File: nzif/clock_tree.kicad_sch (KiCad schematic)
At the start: 63 parts, among them J111 SMA, U128 ABLNO-VCXO, U129 AD9523-1BCPZ, U130 SN74AUC16374DGGR, U131 SN74LVC8T245, U132 SN74CBTLV3253, U133 SN74CBTLV3253, U134 SN74LVC8T245, X101 CTS_535_TCXO

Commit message: wire top sheet from rf front end through rx driver amps
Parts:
- renumbered C233 to C701, C234 to C702, C235 to C703, C236 to C704, C237 to C705, C238 to C706, C239 to C707, C240 to C708, C241 to C709, C242 to C710, C243 to C711, C244 to C712, C245 to C713, C246 to C714, C247 to C715, C248 to C716, C249 to C717, C251 to C718, C252 to C719, C254 to C720, C255 to C721, C250 to C722, C253 to C723, C257 to C724, C258 to C725, C256 to C726, C259 to C727, C260 to C728, C261 to C729, C262 to C730, C264 to C731, C263 to C732, C266 to C733, C265 to C734, C267 to C735, C268 to C736, C269 to C737, C270 to C738, C271 to C739, C272 to C740, C273 to C741, C274 to C742, C275 to C743, C276 to C744, C277 to C745, C278 to C746, C279 to C747, C280 to C748, C281 to C749, J111 to J701, R181 to R701, R182 to R702, R183 to R703, R184 to R704, TR103 to TR701, U128 to U701, U129 to U702, U130 to U703, U131 to U704, U132 to U705, U133 to U706, U134 to U707, X101 to X701

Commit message: updates to top level
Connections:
- net UC_CLK: no longer names the net of U702.53 (OUT4)
- no-connect marks 31 -> 32
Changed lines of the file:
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@@
 	)
 	(no_connect
+		(at 186.69 74.93)
+	)
+	(no_connect
 		(at 186.69 41.91)
 	)
@@
 		)
 	)
-	(hierarchical_label "UC_CLK"
-		(shape output)
-		(at 186.69 74.93 0)
-		(effects
-			(font
-				(size 1.27 1.27)
-			)
-			(justify left)
-		)
-	)

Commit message: minor schematic fixes
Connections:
- net LDO_VCO: now also C726.1
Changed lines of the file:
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@@
-	(wire
-		(pts
-			(xy 69.85 72.39) (xy 81.28 72.39)
-		)
-		(stroke
-			(width 0)
-			(type default)
-		)
-	)
 	(wire
 		(pts
@@
 		(pts
 			(xy 255.27 237.49) (xy 255.27 240.03)
+		)
+		(stroke
+			(width 0)
+			(type default)
+		)
+	)
+	(wire
+		(pts
+			(xy 78.74 72.39) (xy 90.17 72.39)
 		)
 		(stroke
@@
 	)
 	(label "1.8V"
-		(at 123.19 151.13 0)
+		(at 106.68 151.13 0)
 		(effects
 			(font
@@
 	)
 	(label "3.3V"
-		(at 123.19 186.69 0)
-		(effects
-			(font
+		(at 107.95 186.69 0)
+		(effects
+			(font

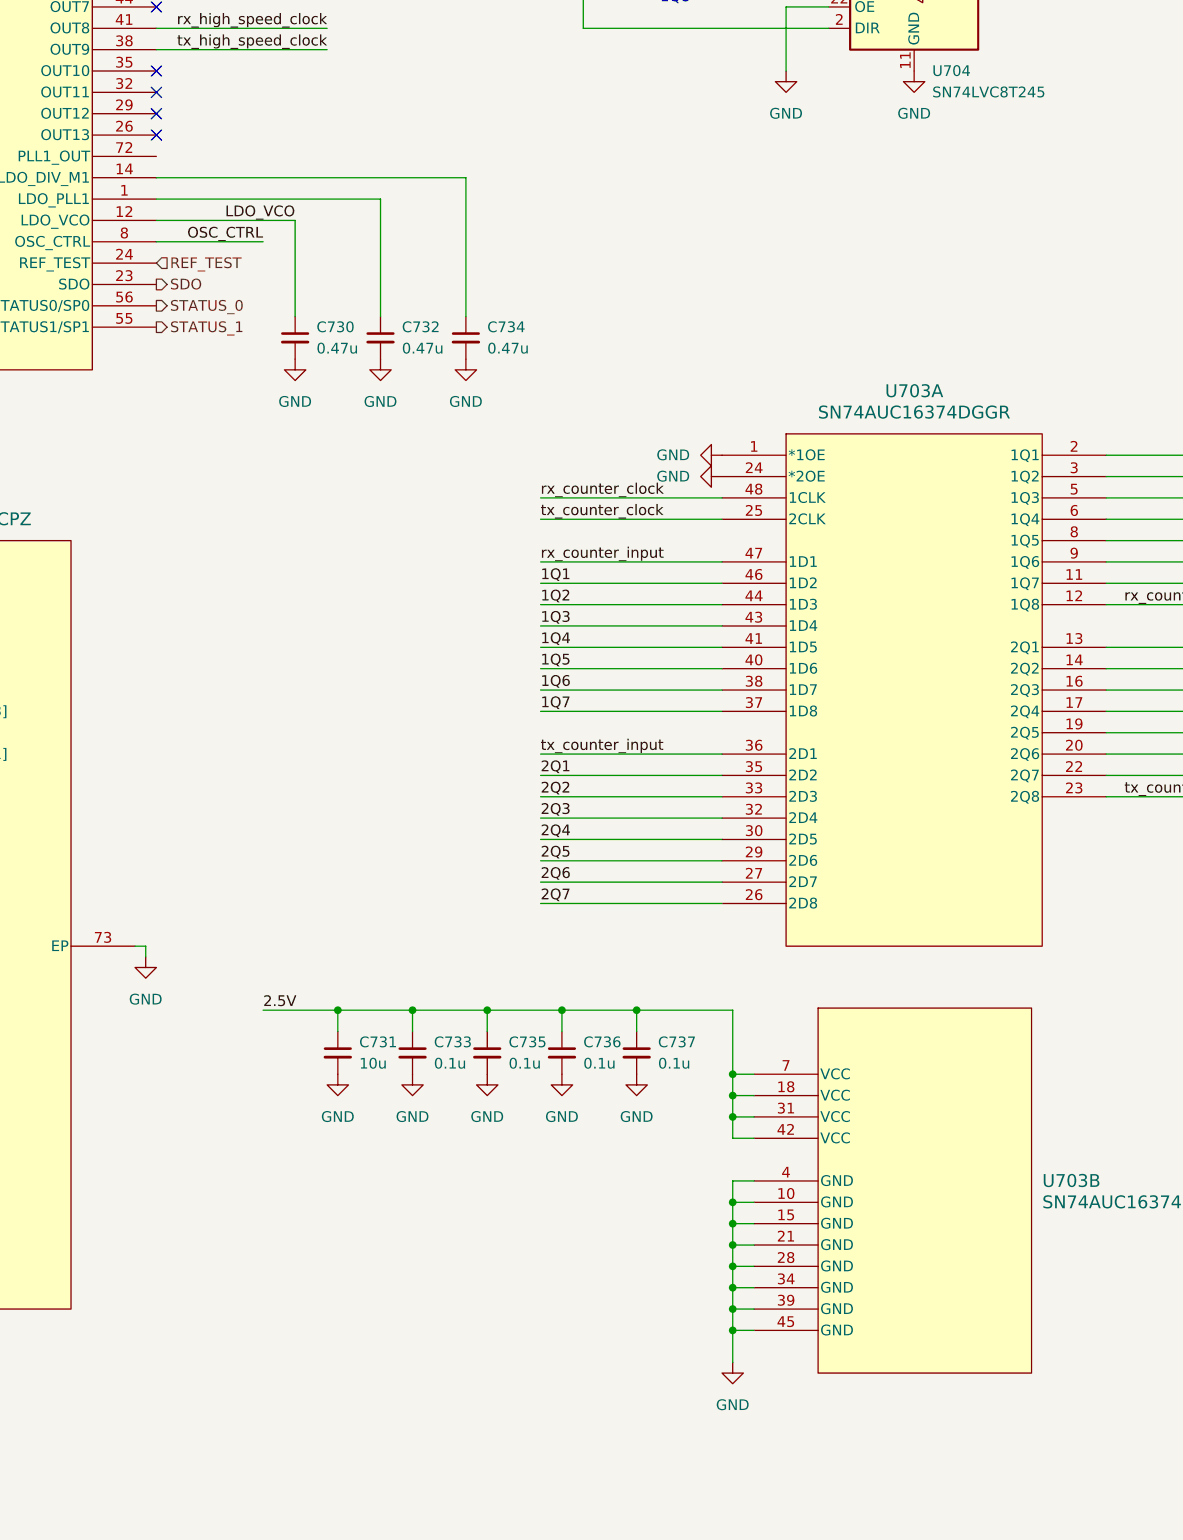
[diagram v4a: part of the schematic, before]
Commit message: Fix ERC errors: symbol pin types and schematic corrections
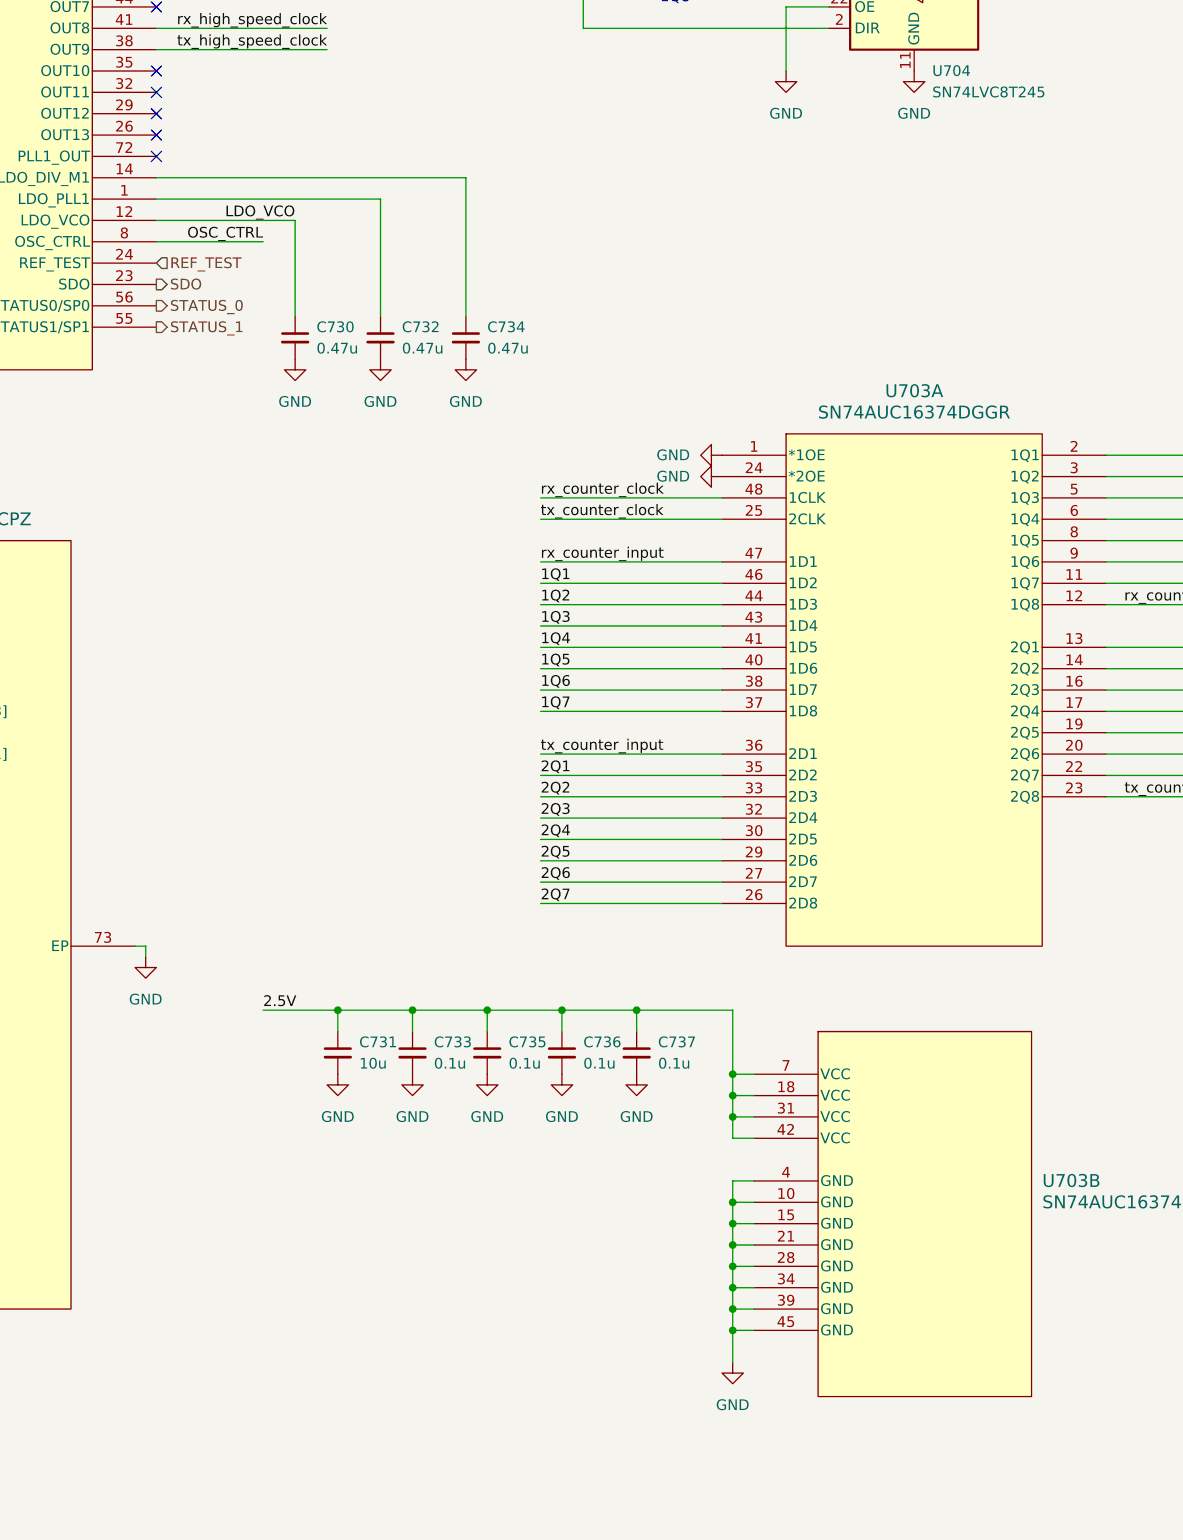
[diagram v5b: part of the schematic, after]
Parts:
- X701: footprint (none) -> nzif_footprints:CTS_535_TCXO
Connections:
- no-connect marks 32 -> 33
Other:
- moved on the sheet: U703B
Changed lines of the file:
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@@
 	)
 	(no_connect
+		(at 186.69 100.33)
+	)
+	(no_connect
 		(at 186.69 62.23)
 	)
@@
 	)
 	(symbol
-		(lib_name "SN74AUC16374DGGR_1")
 		(lib_id "nzif_radio_symbol_library:SN74AUC16374DGGR")
 		(at 257.81 209.55 0)
@@
 			)
 		)
-		(property "Footprint" ""
+		(property "Footprint" "nzif_footprints:CTS_535_TCXO"
 			(at 55.88 127 0)
 			(hide yes)
@@
 			)
 		)
-		(property "Datasheet" ""
+		(property "Datasheet" "https://www.ctscorp.com/"
 			(at 55.88 127 0)
 			(hide yes)

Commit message: fixed remaining ERC errors
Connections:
- net 3V is gone; now on net +3.3V_CLOCKTREE: C748.1, C749.1, U707.23 (V_{CCB}), U707.24 (V_{CCB})
- net PLL1_OUT: now reaches U702.72 (PLL1_OUT)
- net 5V renamed +5V_RX_MIXER
- no-connect marks 33 -> 32
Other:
- note added: "Tx switches are 3.3V"
- note removed: "Tx switches are 3V"
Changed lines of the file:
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@@
 		)
 	)
-	(text "Tx switches are 3V"
+	(text "Tx switches are 3.3V"
 		(exclude_from_sim no)
 		(at 395.732 17.78 0)
 		(effects
 			(font
+				(face "Standard Symbols PS")
 				(size 1.27 1.27)
 			)
@@
 	)
 	(no_connect
-		(at 186.69 100.33)
-	)
-	(no_connect
 		(at 186.69 62.23)
 	)
@@
 	(wire
 		(pts
-			(xy 41.91 27.94) (xy 41.91 35.56)
+			(xy 36.83 24.13) (xy 36.83 31.75)
 		)
 		(stroke
@@
 	(wire
 		(pts
+			(xy 66.04 33.02) (xy 66.04 40.64)
+		)
+		(stroke
+			(width 0)
+			(type default)
+		)
+	)
+	(wire
+		(pts
 			(xy 255.27 217.17) (xy 257.81 217.17)
 		)
@@
 	(wire
 		(pts
-			(xy 21.59 27.94) (xy 21.59 35.56)
+			(xy 21.59 20.32) (xy 21.59 27.94)
 		)
 		(stroke
@@
 	(wire
 		(pts
-			(xy 62.23 27.94) (xy 62.23 35.56)
+			(xy 53.34 27.94) (xy 53.34 35.56)
 		)
 		(stroke
@@
 	)
 	(label "1.8V"
-		(at 21.59 35.56 90)
+		(at 21.59 27.94 90)
 		(effects
 			(font
@@
 	)
 	(label "3.3V"
-		(at 62.23 35.56 90)
+		(at 53.34 35.56 90)
 		(effects
 			(font
@@
 	)
 	(label "2.5V"
-		(at 41.91 35.56 90)
+		(at 36.83 31.75 90)
 		(effects
 			(font
@@
 		)
 	)
+	(label "5V"
+		(at 66.04 40.64 90)
+		(effects
+			(font
+				(size 1.27 1.27)
+			)
+			(justify left bottom)
+		)
+	)
 	(label "rx_counter_clock"
 		(at 232.41 140.97 0)
@@
 		)
 	)
-	(label "3V"
+	(label "3.3V"
 		(at 408.94 20.32 180)
 		(effects
@@
 		)
 	)
+	(hierarchical_label "PLL1_OUT"
+		(shape output)
+		(at 186.69 100.33 0)
+		(effects
+			(font
+				(size 1.27 1.27)
+			)
+			(justify left)
+		)
+	)
 	(hierarchical_label "rx_phase_135"
 		(shape output)
@@
 	(symbol
 		(lib_id "power:+3.3V")
-		(at 62.23 27.94 0)
+		(at 53.34 27.94 0)
 		(unit 1)
 		(body_style 1)
@@
 		(fields_autoplaced yes)
 		(property "Reference" "#PWR0718"
-			(at 62.23 31.75 0)
+			(at 53.34 31.75 0)
 			(hide yes)
 			(show_name no)
@@
 		)
 		(property "Value" "+3.3V_CLOCKTREE"
-			(at 62.23 22.86 0)
+			(at 53.34 22.86 0)
 			(show_name no)
 			(do_not_autoplace no)
@@
 		)
 		(property "Footprint" ""
-			(at 62.23 27.94 0)
+			(at 53.34 27.94 0)
 			(hide yes)
 			(show_name no)
@@
 		)
 		(property "Datasheet" ""
-			(at 62.23 27.94 0)
+			(at 53.34 27.94 0)
 			(hide yes)
 			(show_name no)
@@
 		)
 		(property "Description" "Power symbol creates a global label with name \"+3.3V\""
-			(at 62.23 27.94 0)
+			(at 53.34 27.94 0)
 			(hide yes)
 			(show_name no)
@@
 	(symbol
 		(lib_id "power:+3.3V")
-		(at 41.91 27.94 0)
+		(at 36.83 24.13 0)
 		(unit 1)
 		(body_style 1)
@@
 		(fields_autoplaced yes)
 		(property "Reference" "#PWR0708"
-			(at 41.91 31.75 0)
+			(at 36.83 27.94 0)
 			(hide yes)
 			(show_name no)
@@
 		)
 		(property "Value" "+2.5V_CLOCKTREE"
-			(at 41.91 22.86 0)
+			(at 36.83 19.05 0)
 			(show_name no)
 			(do_not_autoplace no)
@@
 		)
 		(property "Footprint" ""
-			(at 41.91 27.94 0)
+			(at 36.83 24.13 0)
 			(hide yes)
 			(show_name no)
@@
 		)
 		(property "Datasheet" ""
-			(at 41.91 27.94 0)
+			(at 36.83 24.13 0)
 			(hide yes)
 			(show_name no)
@@
 		)
 		(property "Description" "Power symbol creates a global label with name \"+3.3V\""
-			(at 41.91 27.94 0)
+			(at 36.83 24.13 0)
 			(hide yes)
 			(show_name no)
@@
 	(symbol
 		(lib_id "power:+3.3V")
-		(at 21.59 27.94 0)
+		(at 21.59 20.32 0)
 		(unit 1)
 		(body_style 1)
@@
 		(fields_autoplaced yes)
 		(property "Reference" "#PWR0701"
-			(at 21.59 31.75 0)
+			(at 21.59 24.13 0)
 			(hide yes)
 			(show_name no)
@@
 		)
 		(property "Value" "+1.8V_CLOCKTREE"
-			(at 21.59 22.86 0)
+			(at 21.59 15.24 0)
 			(show_name no)
 			(do_not_autoplace no)
@@
 		)
 		(property "Footprint" ""
-			(at 21.59 27.94 0)
+			(at 21.59 20.32 0)
 			(hide yes)
 			(show_name no)
@@
 		)
 		(property "Datasheet" ""
-			(at 21.59 27.94 0)
+			(at 21.59 20.32 0)
 			(hide yes)
 			(show_name no)
@@
 		)
 		(property "Description" "Power symbol creates a global label with name \"+3.3V\""
-			(at 21.59 27.94 0)
+			(at 21.59 20.32 0)
 			(hide yes)
 			(show_name no)
@@
 					(unit 1)
 				)
+			)
+		)
+	)
+	(symbol
+		(lib_id "power:+3.3V")
+		(at 66.04 33.02 0)
+		(unit 1)
+		(body_style 1)
+		(exclude_from_sim no)
+		(in_bom yes)
+		(on_board yes)
+		(in_pos_files yes)
+		(dnp no)
+		(fields_autoplaced yes)
+		(property "Reference" "#PWR0766"
+			(at 66.04 36.83 0)
+			(hide yes)
+			(show_name no)
+			(do_not_autoplace no)
+			(effects
+				(font
+					(size 1.27 1.27)
+				)
+			)
+		)
+		(property "Value" "+5V_RX_MIXER"
+			(at 66.04 27.94 0)
+			(show_name no)
+			(do_not_autoplace no)
+			(effects
+				(font
+					(size 1.27 1.27)
+				)
+			)
+		)
+		(property "Footprint" ""
+			(at 66.04 33.02 0)
+			(hide yes)
+			(show_name no)
+			(do_not_autoplace no)
+			(effects
+				(font
+					(size 1.27 1.27)
+				)
+			)
+		)
+		(property "Datasheet" ""
+			(at 66.04 33.02 0)
+			(hide yes)
+			(show_name no)
+			(do_not_autoplace no)
+			(effects
+				(font
+					(size 1.27 1.27)
+				)
+			)
+		)
+		(property "Description" "Power symbol creates a global label with name \"+3.3V\""
+			(at 66.04 33.02 0)
+			(hide yes)
+			(show_name no)
+			(do_not_autoplace no)
+			(effects
+				(font
+					(size 1.27 1.27)
+				)
+			)
+		)
+		(pin "1"
+		)
+		(instances
+			(project "nzif"
+				(path "/fe42ca2f-2bb8-4d5a-9e84-807788ed632f/79014999-6129-417a-b831-cb9e4a5873fe"
+					(reference "#PWR0766")
+					(unit 1)
+				)

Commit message: update to clocktree
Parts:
- added R1220, R1223, R1224, R1225: 0, symbol Device:R_Small_US
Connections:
- net rx_init_0 is gone; now on net GND: U705.6 (1B1)
- net tx_init_0 is gone; now on net GND: U706.6 (1B1)
- net tx_init_1 is gone; now on net 2.5V: U706.5 (1B2)
- net +1.8V_CLOCKTREE: now also R1220.1; no longer C702.1, C706.1, C711.1, C713.1, C715.1, C717.1, C721.1, C725.1, U702.30 (VDD1.8_OUT[12:13]), U702.36 (VDD1.8_OUT[10:11]), U702.42 (VDD1.8_OUT[8:9]), U702.48 (VDD1.8_OUT[6:7]), U702.54 (VDD1.8_OUT[4:5]), U702.63 (VDD1.8_OUT[0:3]), U702.69 (VDD1.8_PLL2)
- net +2.5V_CLOCKTREE: now also R1223.1; no longer C731.1, C733.1, C735.1, C736.1, C737.1, C738.1, C739.1, C742.1, C743.1, C744.1, C745.1, C746.1, C747.1, R703.1, R704.1, U703.18 (VCC), U703.31 (VCC), U703.42 (VCC), U703.7 (VCC), U704.1 (V_{CCA}), U705.16 (VCC), U706.16 (VCC), U707.1 (V_{CCA})
- net +3.3V_CLOCKTREE: now also R1224.1; no longer C701.1, C703.1, C704.1, C705.1, C707.1, C709.1, C710.1, C712.1, C714.1, C716.1, C720.1, C724.1, C727.1, C728.1, C729.1, C748.1, C749.1, U701.4 (VDD), U702.13 (VDD3_VCO), U702.18 (VDD3_REF), U702.2 (VDD3_PLL1), U702.27 (VDD3_OUT[12:13]), U702.33 (VDD3_OUT[10:11]), U702.39 (VDD3_OUT[8:9]), U702.45 (VDD3_OUT[6:7]), U702.51 (VDD3_OUT[4:5]), U702.60 (VDD3_OUT[2:3]), U702.66 (VDD3_OUT[0:1]), U707.23 (V_{CCB}), U707.24 (V_{CCB}), X701.9 (Vcc)
- net +5V_RX_MIXER: now also R1225.1; no longer C740.1, C741.1, U704.23 (V_{CCB}), U704.24 (V_{CCB})
- net rx_high_speed_clock: now also U705.12 (2B3), U705.13 (2B4); no longer U705.11 (2B2)
- net tx_high_speed_clock: now also U706.12 (2B3), U706.13 (2B4); no longer U706.11 (2B2)
- net rx_init_1 renamed 2.5V
- net 2.5V: now also C731.1, C733.1, C735.1, C736.1, C737.1, C738.1, C739.1, C742.1, C743.1, C744.1, C745.1, C746.1, C747.1, R703.1, R704.1, U703.18 (VCC), U703.31 (VCC), U703.42 (VCC), U703.7 (VCC), U704.1 (V_{CCA}), U705.16 (VCC), U706.16 (VCC), U707.1 (V_{CCA}), R1223.2
- net rx_init_clock renamed RX_INIT_CLK
- net RX_INIT_CLK: now also U705.11 (2B2)
- net tx_init_clock renamed TX_INIT_CLK
- net TX_INIT_CLK: now also U706.11 (2B2)
- new net 1.8V: C702.1, C706.1, C711.1, C713.1, C715.1, C717.1, C721.1, C725.1, R1220.2, U702.30 (VDD1.8_OUT[12:13]), U702.36 (VDD1.8_OUT[10:11]), U702.42 (VDD1.8_OUT[8:9]), U702.48 (VDD1.8_OUT[6:7]), U702.54 (VDD1.8_OUT[4:5]), U702.63 (VDD1.8_OUT[0:3]), U702.69 (VDD1.8_PLL2)
- new net 3.3V: C701.1, C703.1, C704.1, C705.1, C707.1, C709.1, C710.1, C712.1, C714.1, C716.1, C720.1, C724.1, C727.1, C728.1, C729.1, C748.1, C749.1, R1224.2, U701.4 (VDD), U702.13 (VDD3_VCO), U702.18 (VDD3_REF), U702.2 (VDD3_PLL1), U702.27 (VDD3_OUT[12:13]), U702.33 (VDD3_OUT[10:11]), U702.39 (VDD3_OUT[8:9]), U702.45 (VDD3_OUT[6:7]), U702.51 (VDD3_OUT[4:5]), U702.60 (VDD3_OUT[2:3]), U702.66 (VDD3_OUT[0:1]), U707.23 (V_{CCB}), U707.24 (V_{CCB}), X701.9 (Vcc)
- new net 5V: C740.1, C741.1, R1225.2, U704.23 (V_{CCB}), U704.24 (V_{CCB})
- no-connect marks 32 -> 28

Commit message: updated clocktree and associated section of README.md
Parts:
- added C750, C752: 10u, symbol Device:C_Small
- added C751, C753: 0.1u, symbol Device:C_Small
- added R1226: 10k, symbol Device:R_Small_US
- added R1227: 33k, symbol Device:R_Small_US
- added U1204, U1205: SN74AUC08RGYR, nzif_footprints:RGY14_2P05X2P05, symbol nzif_radio_symbol_library:SN74AUC08RGYR
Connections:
- net 1Q5: now also U1204.4 (2A); no longer U703.40 (1D6)
- net 1Q6: now also U1204.9 (3A); no longer U703.38 (1D7)
- net 1Q7: now also U1204.12 (4A); no longer U703.37 (1D8)
- net 2.5V: now also C750.1, C751.1, C752.1, C753.1, U1204.14 (VCC), U1205.14 (VCC)
- net 2Q1: now also U707.3 (A1)
- net 2Q2: no longer U707.3 (A1)
- net 2Q5: now also U1205.4 (2A); no longer U703.29 (2D6)
- net 2Q6: now also U1205.9 (3A); no longer U703.27 (2D7)
- net 2Q7: now also U1205.12 (4A); no longer U703.26 (2D8)
- net GND: now also C750.2, C751.2, C752.2, C753.2, R1227.2, U1204.15 (EPAD), U1204.7 (GND), U1205.15 (EPAD), U1205.7 (GND)
- net tx_counter_feedback_8: now reaches U706.3 (1B4)
- net tx_counter_feedback_8: now also U703.23 (2Q8), U707.10 (A8)
- net rx_counter_feedback_8: now reaches U705.3 (1B4)
- net rx_counter_feedback_8: now also U703.12 (1Q8), U704.10 (A8)
- net 1Q4 renamed rx_counter_feedback_4
- net rx_counter_feedback_4: now also U705.4 (1B3), U1204.1 (1A); no longer U703.41 (1D5)
- net 2Q4 renamed tx_counter_feedback_4
- net tx_counter_feedback_4: now also U706.4 (1B3), U1205.1 (1A); no longer U703.30 (2D5)
- removed net rx_counter_feedback: U703.12 (1Q8), U704.10 (A8), U705.4 (1B3)
- removed net tx_counter_feedback: U703.23 (2Q8), U706.4 (1B3), U707.10 (A8)
- new net 1D5: U1204.3 (1Y), U703.41 (1D5)
- new net 1D6: U1204.6 (2Y), U703.40 (1D6)
- new net 1D7: U1204.8 (3Y), U703.38 (1D7)
- new net 1D8: U1204.11 (4Y), U703.37 (1D8)
- new net 2D4: U703.30 (2D5)
- new net 2D5: U1205.3 (1Y), U703.29 (2D6)
- new net 2D6: U1205.6 (2Y), U703.27 (2D7)
- new net 2D7: U1205.8 (3Y), U703.26 (2D8)
- new net 2D8: U1205.11 (4Y)
- new net PHASE_SEL_8: R1226.1
- new net sel_8: R1226.2, R1227.1, U1204.10 (3B), U1204.13 (4B), U1204.2 (1B), U1204.5 (2B), U1205.10 (3B), U1205.13 (4B), U1205.2 (1B), U1205.5 (2B)
- no-connect marks 28 -> 26
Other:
- note added: "1Q4"
- note added: "2Q4"
- moved on the sheet: C703, C704, C707, C708, C709, C718, C719, C731, C733, C735, C736, C737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
